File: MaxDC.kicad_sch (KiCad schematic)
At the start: 32 parts, among them J1 L N E, J2 Screw_Terminal_01x04, T2 70063K

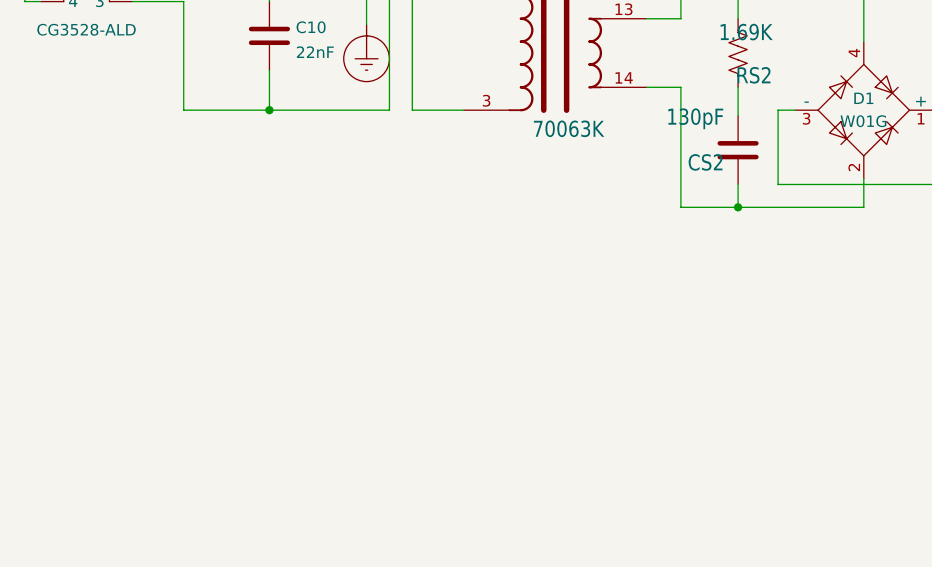
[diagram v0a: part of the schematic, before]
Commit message: Add files via upload
Uploaded to JLC.   Branch ready to merge back to main.
Move edge to the left and change width to 99.5mm.   After checking a 100mm board in a 1455 case, I made this board .5mm wider.   Move the edges to give the transformer a little more clearance. 
Moved the caps at the bottom of the board up 1mm.  That is to give more clearance for output connectors.    5-way binding posts should clear, but this gives a little more leeway.
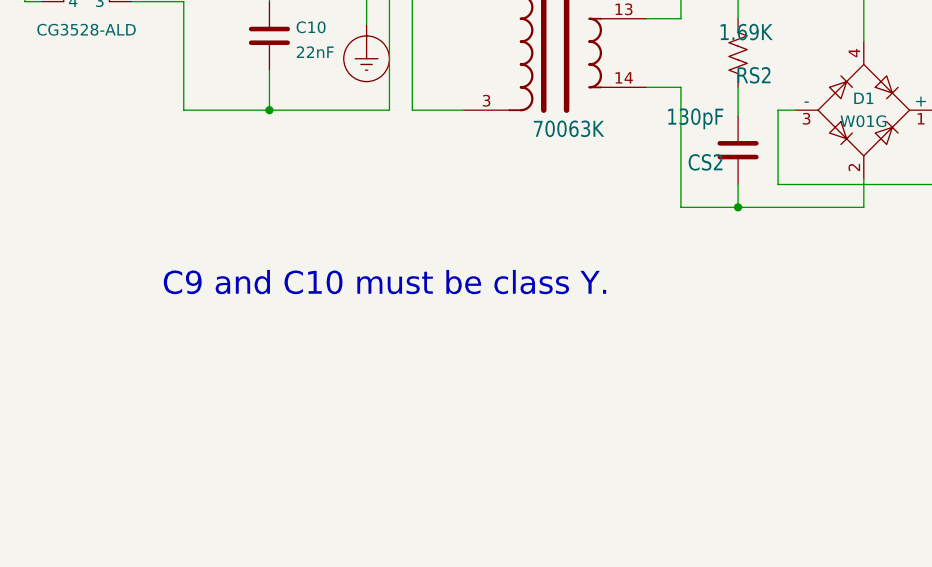
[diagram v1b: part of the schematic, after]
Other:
- note added: "C9 and C10 must be class Y."
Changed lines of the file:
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@@
   (title_block
     (title "MaxDC")
-    (date "2023-01-24")
-    (rev "0.2")
+    (date "2023-01-28")
+    (rev "0.3")
     (company "Author: Andrew Fischer\\nLicense: CC BY-NC 4.0 \\ncreativecommons.org/licenses/by-nc/4.0")
   )
@@
     (stroke (width 0) (type default) (color 0 0 0 0))
   )
+  (text "C9 and C10 must be class Y." (at 70.612 120.65 0)
+    (effects (font (size 2.54 2.54)) (justify left bottom))
+  )
   (global_label "T4" (shape input) (at 215.265 76.835 0) (fields_autoplaced)
